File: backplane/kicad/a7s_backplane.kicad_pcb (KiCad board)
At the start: 2 copper layers, 86.2 x 74.1 mm, 26 parts, among them J1 Conn_02x15_Odd_Even, J10 ENC, J11 BTN5_6, J12 FLIPPER, J2 Conn_01x15, J3 Conn_01x14, J5 Conn_02x04_Odd_Even, J5b Conn_01x01, J6 Conn_02x04_Odd_Even, J6b Conn_01x01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

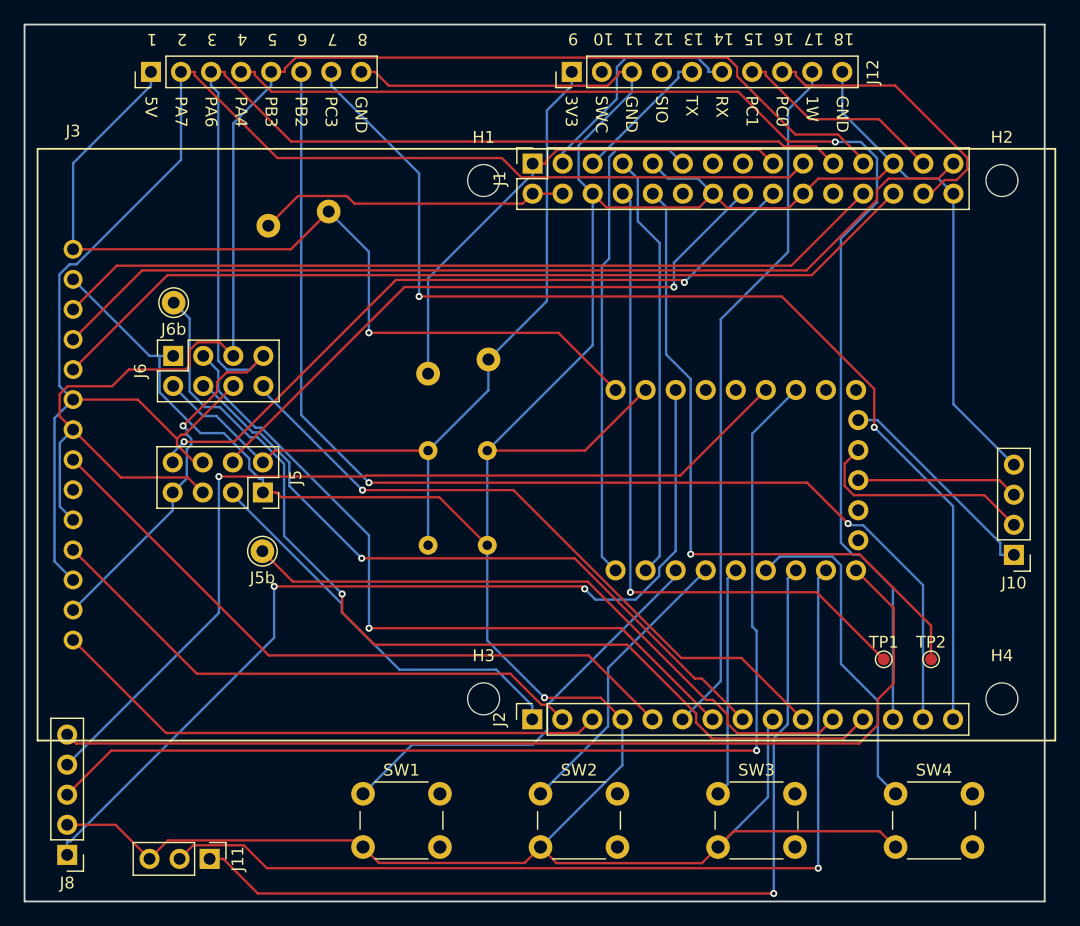
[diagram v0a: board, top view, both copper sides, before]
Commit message: backplane: headers to back, Flipper female socket, inputs as solder pads; exploded assembly render with A7S; drop old half-view renders
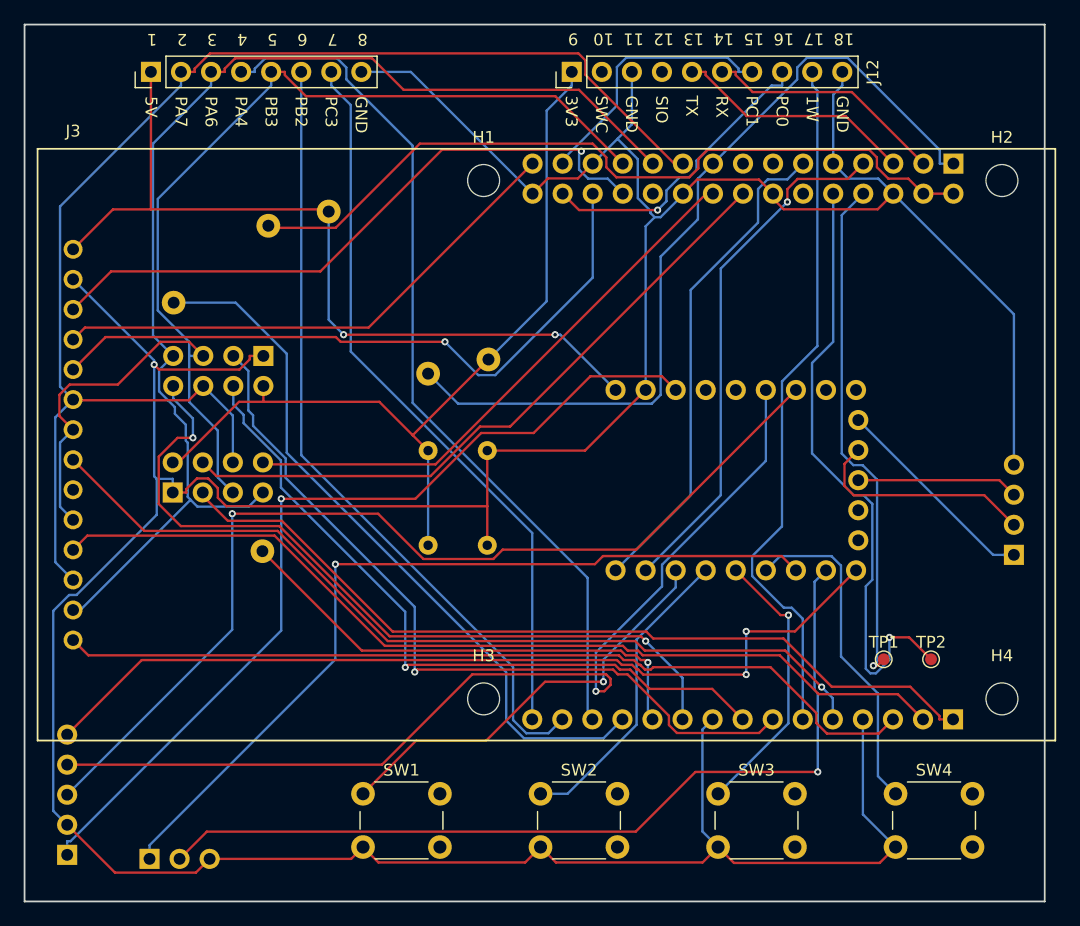
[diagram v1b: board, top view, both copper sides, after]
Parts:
- J1, J10, J11, J2, J5, J5b, J6, J6b, J8: moved to B.Cu
- moved J1 35.6 mm to (79.9, 31.8)
- moved J2 35.6 mm to (79.9, 78.7)
- moved J5 7.62 mm to (13.9, 59.5)
- moved J6 7.62 mm to (21.6, 48.0)
- moved J11 5.08 mm to (12.0, 90.5)
- turned J10 to 0 degrees
- turned J5b to 180 degrees
- turned J6b to 180 degrees
- turned J8 to 0 degrees
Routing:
- net +5V_IN: track 26.5 -> 66.0 mm
- net RADIO1_FLEXA: track 34.4 -> 71.7 mm
- net TFT_RST: track 81.0 -> 45.0 mm
- net SPARE0: track 107.8 -> 73.5 mm, vias 1 -> 0
- net SPARE2: track 94.4 -> 61.7 mm, vias 2 -> 0
- net SPARE1: track 98.8 -> 67.3 mm, vias 2 -> 0
- net TOUCH_CS: track 47.3 -> 78.7 mm
- net +3V3_IN: track 43.0 -> 71.4 mm
- net TOUCH_IRQ: track 47.6 -> 73.7 mm
- net RADIO2_AUX: track 82.7 -> 61.1 mm, vias 1 -> 0
- net SPI_SCK: track 123.3 -> 102.9 mm
- net TFT_DC: track 75.5 -> 56.9 mm, vias 0 -> 1
- net TFT_BL: track 58.0 -> 74.3 mm, vias 0 -> 1
- net TFT_CS: track 70.8 -> 54.8 mm, vias 0 -> 1
- net CONSOLE_TX: track 57.7 -> 43.6 mm
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
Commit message: backplane: right-handed layout (A7S inverted, USB-C left); radios 90deg top-right; routed 0-unconnected; new renders
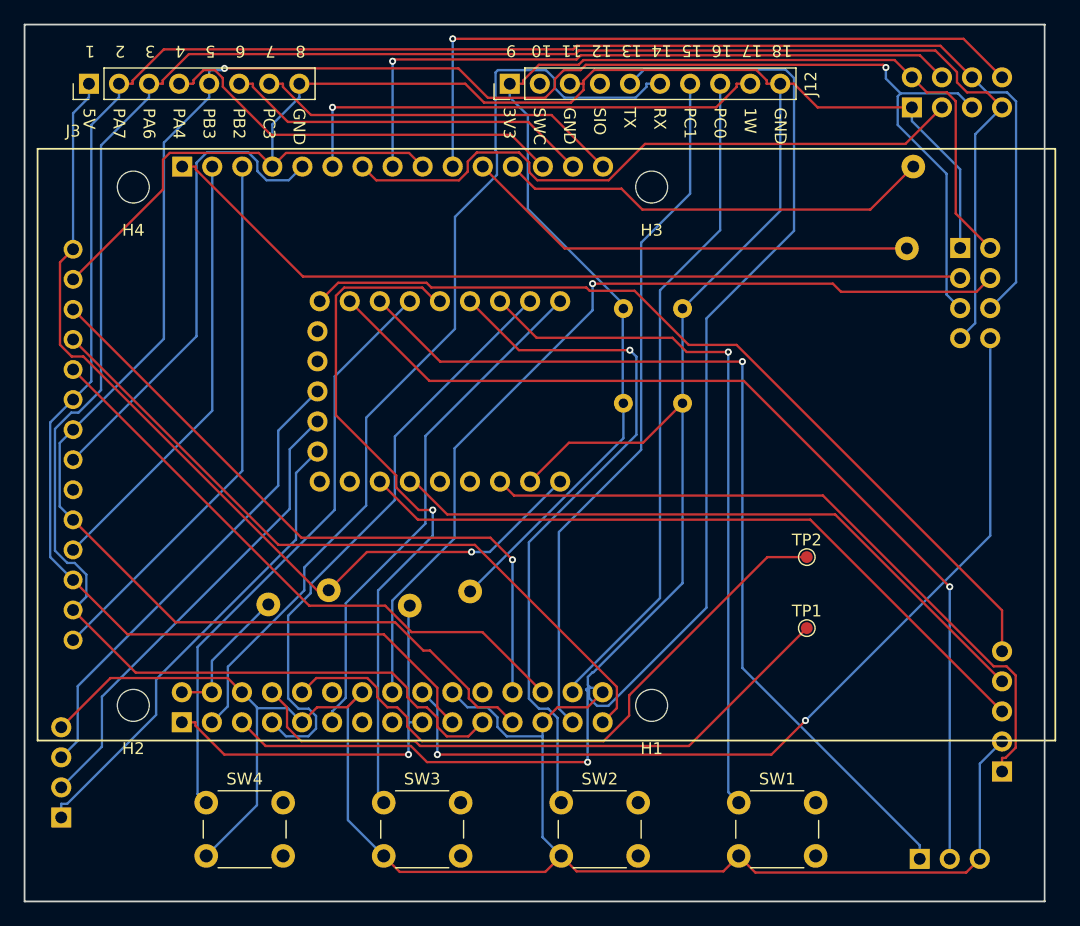
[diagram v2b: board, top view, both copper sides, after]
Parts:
- moved H2 85.8 mm to (10.6, 77.5), turned to 180 degrees
- moved H4 85.2 mm to (10.6, 33.7), turned to 180 degrees
- moved J10 83.5 mm to (4.50, 87.0)
- moved J1 80.5 mm to (14.7, 79.0), turned to -90 degrees
- moved J2 80.2 mm to (14.7, 32.0), turned to -90 degrees
- moved J8 79.3 mm to (84.0, 83.1)
- moved J5 69.7 mm to (80.5, 38.9), turned to 180 degrees
- moved J11 65.1 mm to (77.0, 90.5)
- moved J6b 63.5 mm to (76.5, 32.0)
- moved J5b 60.2 mm to (76.0, 38.9), turned to 90 degrees
- moved J6 58.7 mm to (76.4, 27.0), turned to -90 degrees
- moved SW4 58.3 mm to (16.8, 85.8)
- moved H1 46.6 mm to (54.4, 77.5), turned to 180 degrees
- moved H3 45.5 mm to (54.4, 33.7), turned to 180 degrees
- moved F1 32.0 mm to (22.0, 69.0)
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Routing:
- net UART3_TX: track 20.4 -> 114.1 mm, vias 0 -> 1
- net SPI_MISO: track 102.8 -> 187.3 mm
- net SPI_SCK: track 102.9 -> 178.0 mm, vias 0 -> 2
- net SPI_MOSI: track 115.7 -> 180.7 mm
- net UART3_RX: track 20.4 -> 81.0 mm
- net +5V_IN: track 66.0 -> 11.9 mm
- net TOUCH_CS: track 78.7 -> 37.3 mm
- net SPARE0: track 73.5 -> 35.2 mm
- net +3V3_IN: track 71.4 -> 34.2 mm, vias 0 -> 1
- net I2C_SDA: track 22.5 -> 59.0 mm
- net SPARE1: track 67.3 -> 31.3 mm
- net BTN3: track 23.6 -> 58.6 mm
- net +3V3: track 71.0 -> 106.0 mm
- net TFT_BL: track 74.3 -> 40.7 mm, vias 1 -> 0
- net BTN2: track 26.0 -> 59.0 mm, vias 0 -> 1
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
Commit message: backplane: validated radio spacing (6.3mm module clearance), re-routed 0-unconnected; board-only renders + module keep-out on Dwgs.User
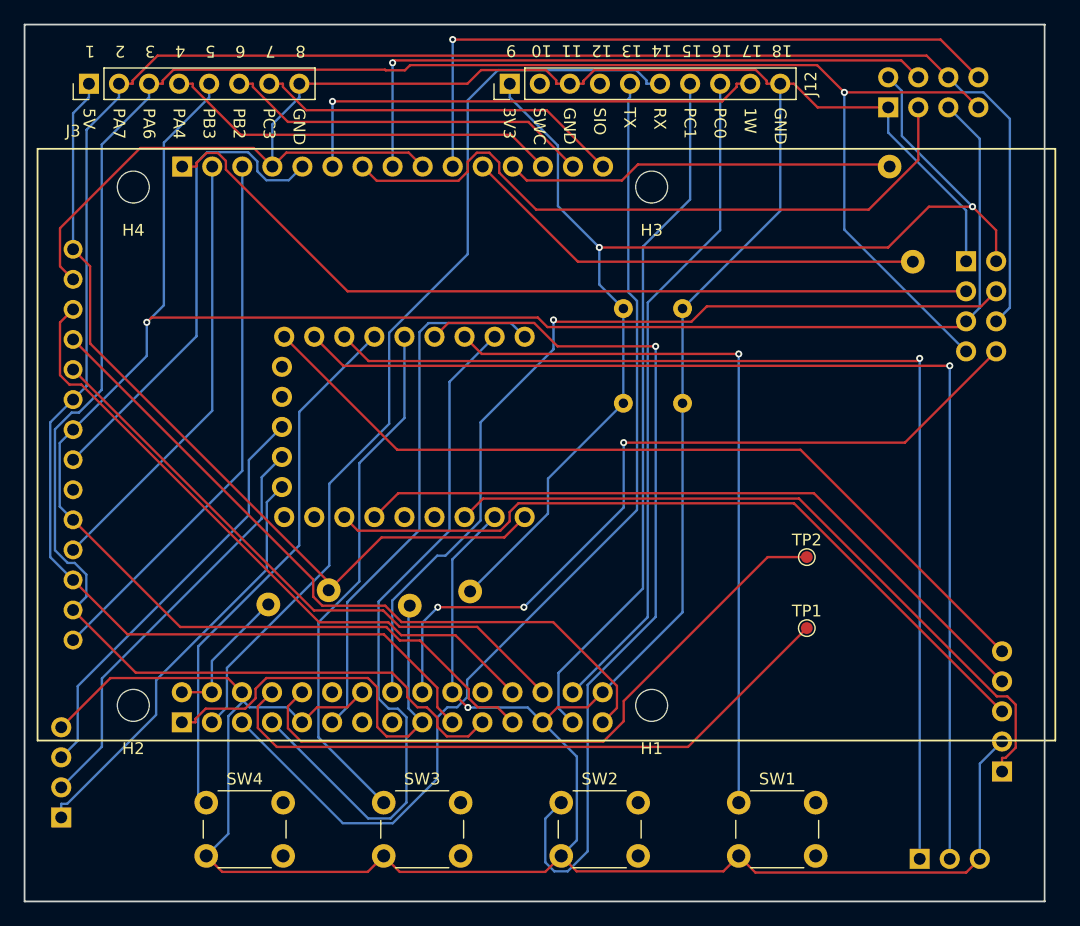
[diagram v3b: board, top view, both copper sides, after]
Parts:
- moved A1 4.24 mm to (33.5, 54.0)
- moved J6 2.00 mm to (74.4, 27.0)
- moved J6b 2.00 mm to (74.5, 32.0)
- moved J5 1.23 mm to (81.0, 40.0)
- moved J5b 1.23 mm to (76.5, 40.0)
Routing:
- net UART3_TX: track 114.1 -> 88.2 mm, vias 1 -> 0
- net BTN2: track 59.0 -> 75.2 mm
- net BTN3: track 58.6 -> 44.7 mm, vias 1 -> 0
- net BTN6: track 83.7 -> 96.4 mm
- net BTN5: track 81.0 -> 91.9 mm
- net RADIO1_FLEXB: track 76.9 -> 67.1 mm, vias 2 -> 3
- net A7S_U2TX: track 50.5 -> 60.1 mm
- net +5V: track 77.7 -> 71.2 mm, vias 1 -> 0
- net BTN4: track 50.1 -> 45.8 mm
- net ENC_B: track 39.9 -> 35.6 mm
- net ENC_A: track 40.2 -> 35.9 mm
- net ENC_SW: track 39.9 -> 35.6 mm
- net JOY_X: track 60.6 -> 64.8 mm
- net RADIO2_AUX: track 36.8 -> 33.0 mm
- net JOY_Y: track 57.0 -> 60.5 mm
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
